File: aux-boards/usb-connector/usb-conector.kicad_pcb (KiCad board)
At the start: 4 copper layers, 35.2 x 31.2 mm, 2 parts, among them J5 Conn_02x12_Odd_Even

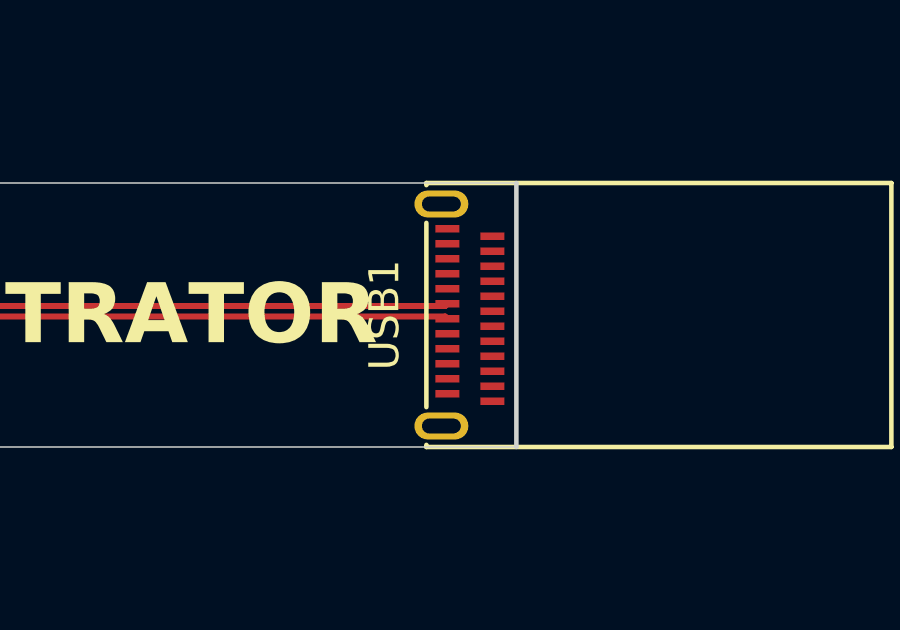
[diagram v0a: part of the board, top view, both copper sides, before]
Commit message: Add fanout
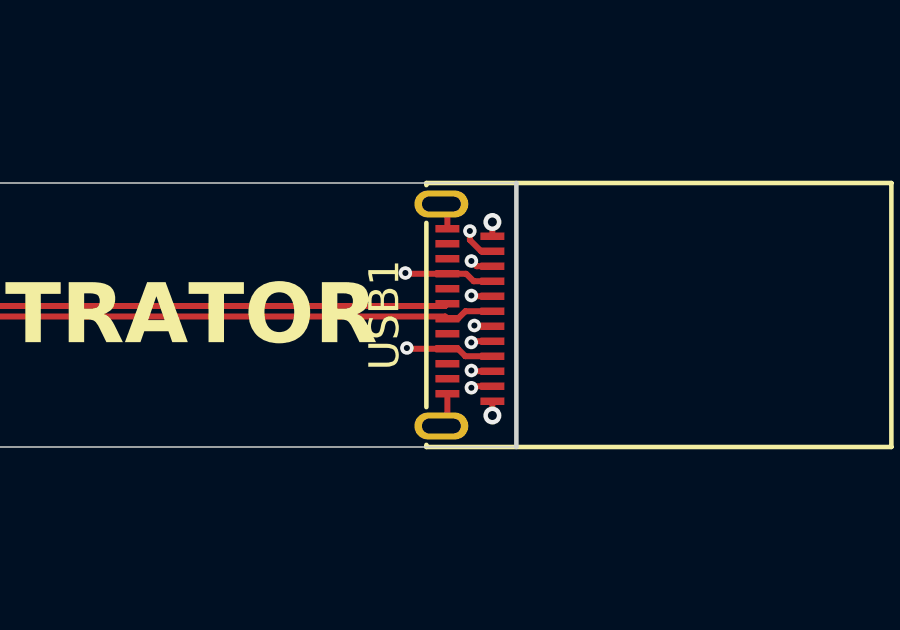
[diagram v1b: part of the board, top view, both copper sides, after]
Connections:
- USB1 pad B6: unconnected-(USB1-DP2-PadB6) -> PRE_USB_TARGET_D+
- USB1 pad B7: unconnected-(USB1-DN2-PadB7) -> PRE_USB_TARGET_D-
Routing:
- net TARGET_USB_VBUS: track 0.00 -> 5.98 mm, vias 0 -> 2
- net GND: track 0.00 -> 3.02 mm, vias 0 -> 2
- net PRE_USB_TARGET_D-: track 29.2 -> 30.8 mm
- net USB_D3: track 0.00 -> 1.21 mm, vias 0 -> 1
- net USB_D2: track 0.00 -> 0.77 mm, vias 0 -> 1
- net USB_D4: track 0.00 -> 0.72 mm, vias 0 -> 1
- net USB_TARGET_CC2: track 0.00 -> 0.72 mm, vias 0 -> 1
- net USB_D9: track 0.00 -> 0.71 mm, vias 0 -> 1
- net USB_D5: track 0.00 -> 0.71 mm, vias 0 -> 1
- net PRE_USB_TARGET_D+: track 29.2 -> 29.8 mm, vias 1 -> 2

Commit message: run autoroute
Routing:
- net USB_D0: track 0.00 -> 64.6 mm, vias 0 -> 1
- net USB_D7: track 0.00 -> 49.6 mm, vias 0 -> 1
- net USB_D1: track 0.00 -> 42.1 mm, vias 0 -> 2
- net USB_D6: track 0.00 -> 35.5 mm
- net USB_D4: track 0.72 -> 34.0 mm
- net USB_D3: track 1.21 -> 34.3 mm, vias 1 -> 2
- net USB_TARGET_CC2: track 0.72 -> 33.7 mm
- net USB_D5: track 0.71 -> 33.4 mm, vias 1 -> 2
- net USB_D2: track 0.77 -> 33.3 mm
- net USB_D9: track 0.71 -> 31.8 mm
- net USB_TARGET_CC1: track 0.00 -> 28.8 mm, vias 0 -> 1
- net USB_D8: track 0.00 -> 28.0 mm

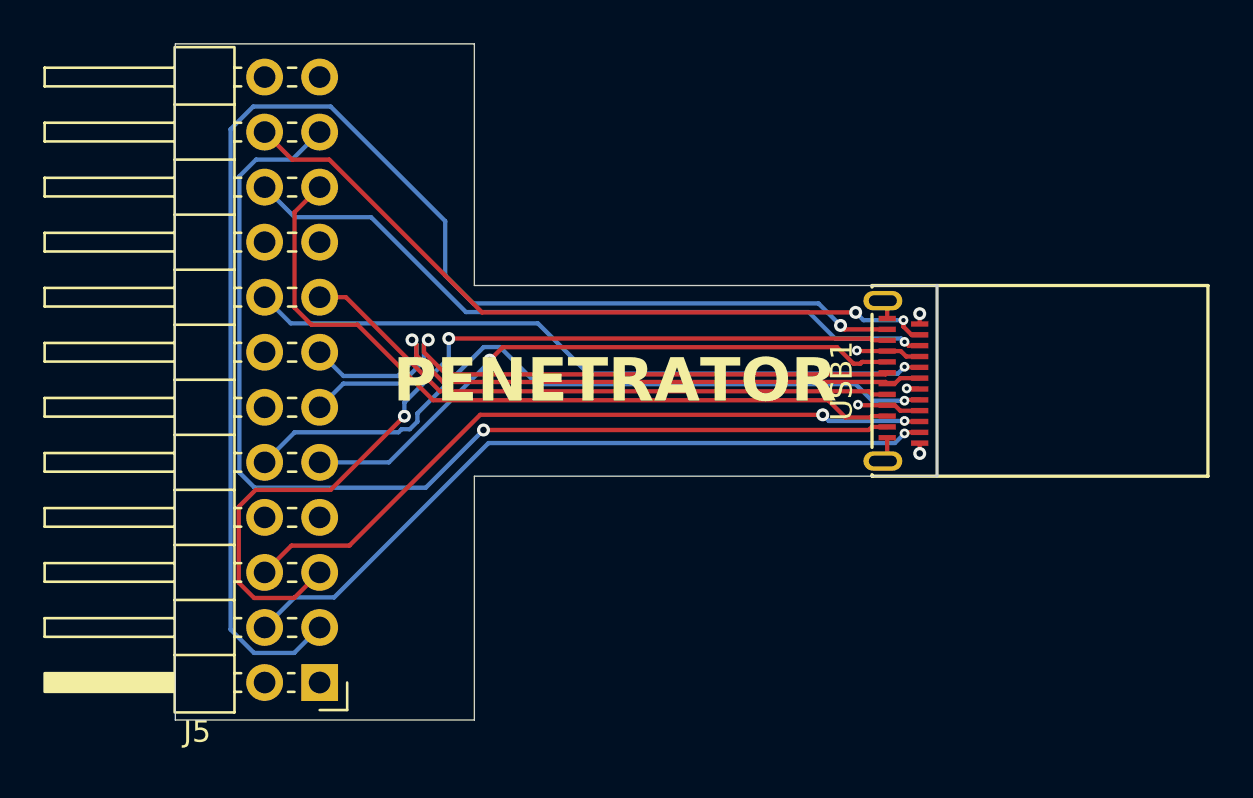
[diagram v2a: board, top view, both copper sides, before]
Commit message: finish usb connector
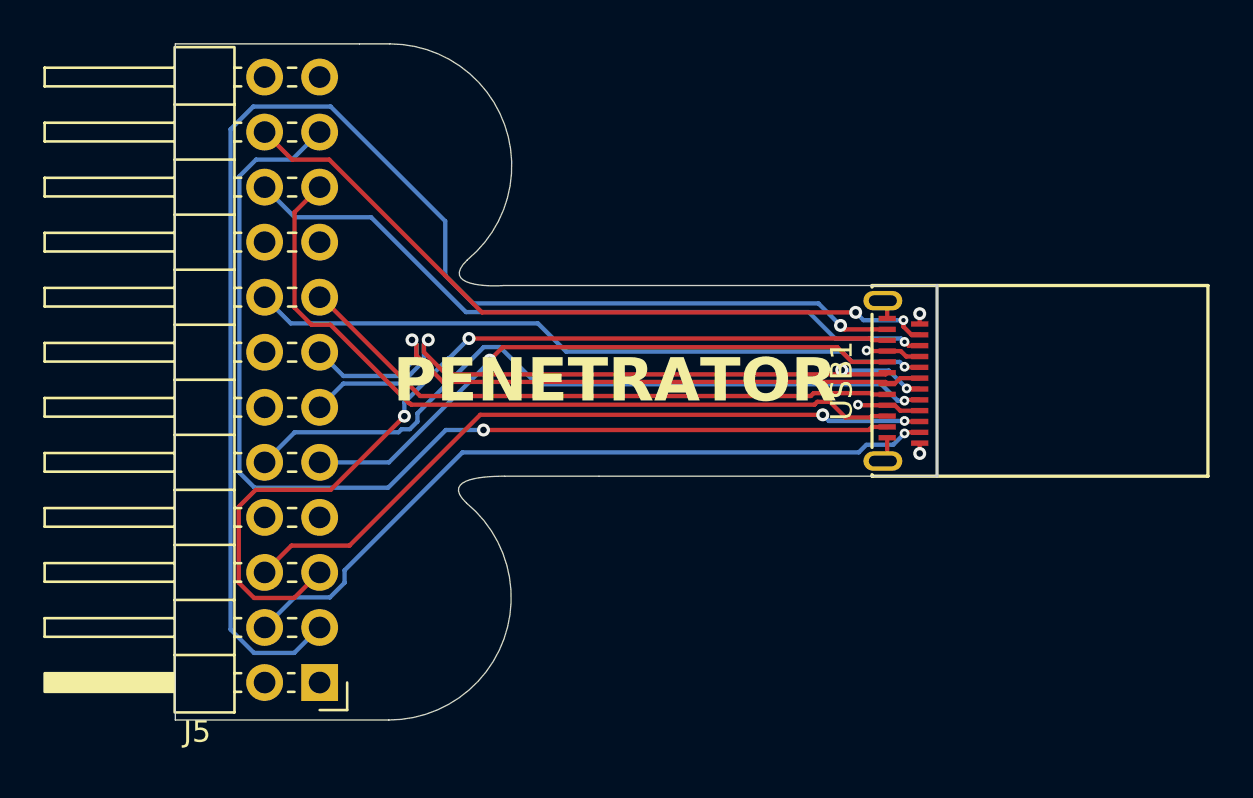
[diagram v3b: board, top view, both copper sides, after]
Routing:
- net PRE_USB_TARGET_D+: track 29.8 -> 33.2 mm, vias 2 -> 3
- net USB_D1: track 42.1 -> 41.6 mm
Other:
- outline, holes or cut-outs redrawn
